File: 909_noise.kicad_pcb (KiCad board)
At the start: 2 copper layers, 30 x 20 mm, 20 parts, among them J1 Conn_01x02_Pin, J2 Conn_01x03_Pin, J3 3220-10-0300-00, SW1 PTS645SM43SMTR92 LFS, U1 STM32G030J6Mx, U2 L78L33ABUTR, U3 TLV7211A

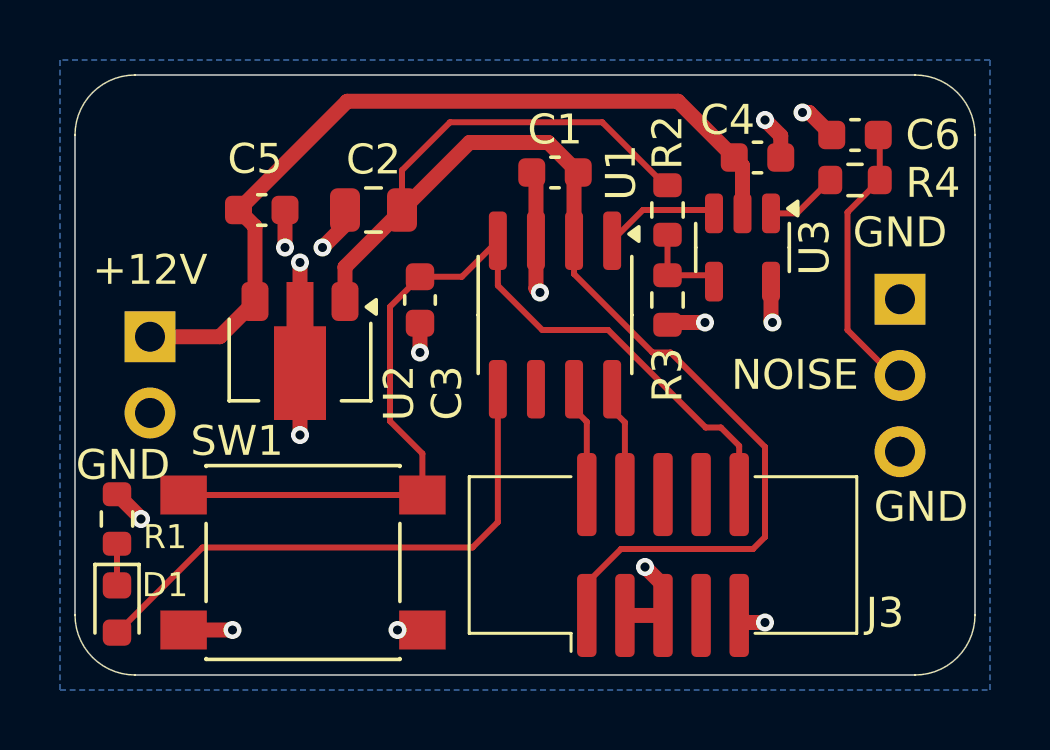
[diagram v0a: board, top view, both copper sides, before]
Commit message: cleanup footprint attributes between pcb and sch
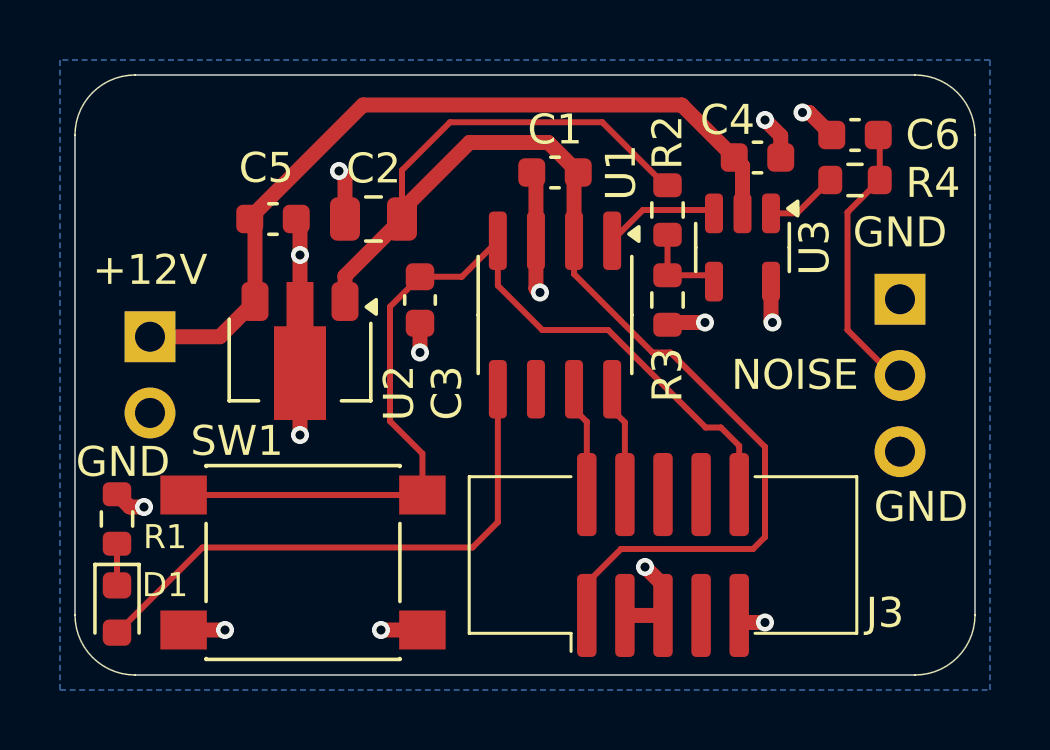
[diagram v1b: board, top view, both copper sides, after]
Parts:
- moved C5 0.48 mm to (51.6, 24.8)
- moved C2 0.30 mm to (55.0, 24.8)
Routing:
- net +12V: track 28.0 -> 27.2 mm
- net GND: track 26.8 -> 27.4 mm, vias 15 -> 14
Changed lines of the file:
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@@
 	(footprint "Capacitor_SMD:C_0603_1608Metric"
 		(layer "F.Cu")
-		(at 51.225 24.5 180)
+		(at 51.6 24.8 180)
 		(descr "Capacitor SMD 0603 (1608 Metric), square (rectangular) end terminal, IPC_7351 nominal, (Body size source: IPC-SM-782 page 76, https://www.pcb-3d.com/wordpress/wp-content/uploads/ipc-sm-782a_amendment_1_and_2.pdf), generated with kicad-footprint-generator")
 		(tags "capacitor")
@@
 	(footprint "Capacitor_SMD:C_0805_2012Metric"
 		(layer "F.Cu")
-		(at 54.95 24.5)
+		(at 54.95 24.8)
 		(descr "Capacitor SMD 0805 (2012 Metric), square (rectangular) end terminal, IPC_7351 nominal, (Body size source: IPC-SM-782 page 76, https://www.pcb-3d.com/wordpress/wp-content/uploads/ipc-sm-782a_amendment_1_and_2.pdf, https://docs.google.com/spreadsheets/d/1BsfQQcO9C6DZCsRaXUlFlo91Tg2WpOkGARC1WS5S8t0/edit?usp=sharing), generated with kicad-footprint-generator")
 		(tags "capacitor")
@@
 		(sheetname "Root")
 		(sheetfile "909_noise.kicad_sch")
-		(attr through_hole)
+		(attr exclude_from_pos_files exclude_from_bom allow_missing_courtyard)
 		(fp_poly
 			(pts
@@
 		)
 		(property "pin2" "GND"
-			(at 0.9 -4.275 0)
+			(at 0.9 -4.175 0)
 			(unlocked yes)
 			(layer "F.SilkS")
@@
 	)
 	(segment
-		(start 54 25)
-		(end 53.25 25.75)
+		(start 50 38.5)
+		(end 48.62 38.5)
 		(width 0.5)
 		(layer "F.Cu")
@@
 	)
 	(segment
-		(start 52.5 27.6375)
-		(end 52.5 26.25)
+		(start 68.2 26.8875)
+		(end 68.2 28.2)
 		(width 0.5)
 		(layer "F.Cu")
@@
 	)
 	(segment
-		(start 55.75 38.5)
-		(end 56.58 38.5)
+		(start 52.5 27.6375)
+		(end 52.5 32)
 		(width 0.5)
 		(layer "F.Cu")
@@
 	)
 	(segment
-		(start 54 24.5)
-		(end 54 25)
+		(start 69.25 21.25)
+		(end 69.475 21.25)
 		(width 0.5)
 		(layer "F.Cu")
@@
 	)
 	(segment
-		(start 68.2 26.8875)
-		(end 68.2 28.2)
+		(start 55.2 38.5)
+		(end 56.58 38.5)
 		(width 0.5)
 		(layer "F.Cu")
@@
 	)
 	(segment
-		(start 52.5 27.6375)
-		(end 52.5 32)
+		(start 54 24.8)
+		(end 53.95 24.8)
 		(width 0.5)
 		(layer "F.Cu")
@@
 	)
 	(segment
-		(start 69.25 21.25)
-		(end 69.475 21.25)
+		(start 64.6 37)
+		(end 64.6 38.015)
 		(width 0.5)
 		(layer "F.Cu")
@@
 	)
 	(segment
-		(start 64.6 37)
-		(end 64.6 38.015)
+		(start 60.365 27.115)
+		(end 60.5 27.25)
 		(width 0.5)
 		(layer "F.Cu")
@@
 	)
 	(segment
-		(start 60.365 27.115)
-		(end 60.5 27.25)
+		(start 52.5 27.6375)
+		(end 52.5 26)
 		(width 0.5)
 		(layer "F.Cu")
@@
 	)
 	(segment
-		(start 50.25 38.5)
-		(end 48.62 38.5)
-		(width 0.5)
-		(layer "F.Cu")
-		(net 1)
-	)
-	(segment
-		(start 47.2 34.775)
-		(end 46.4 33.975)
+		(start 47.3 34.4)
+		(end 46.825 34.4)
 		(width 0.5)
 		(layer "F.Cu")
@@
 	)
 	(segment
-		(start 47.2 34.8)
-		(end 47.2 34.775)
-		(width 0.5)
-		(layer "F.Cu")
-		(net 1)
-	)
-	(segment
 		(start 68.2 28.2)
 		(end 68.25 28.25)
@@
 	)
 	(segment
+		(start 54 24.8)
+		(end 54 23.4)
+		(width 0.5)
+		(layer "F.Cu")
+		(net 1)
+	)
+	(segment
 		(start 64.9 28.25)
 		(end 64.825 28.325)
@@
 	)
 	(segment
+		(start 54 23.4)
+		(end 53.8 23.2)
+		(width 0.5)
+		(layer "F.Cu")
+		(net 1)
+	)
+	(segment
+		(start 52.5 26)
+		(end 52.5 24.925)
+		(width 0.5)
+		(layer "F.Cu")
+		(net 1)
+	)
+	(segment
 		(start 69.475 21.25)
 		(end 70.225 22)
@@
 	)
 	(segment
-		(start 52 24.5)
-		(end 52 25.75)
+		(start 46.825 34.4)
+		(end 46.4 33.975)
+		(width 0.5)
+		(layer "F.Cu")
+		(net 1)
+	)
+	(segment
+		(start 52.5 24.925)
+		(end 52.375 24.8)
 		(width 0.5)
 		(layer "F.Cu")
@@
 	)
 	(via
-		(at 50.25 38.5)
+		(at 50 38.5)
 		(size 0.6)
 		(drill 0.3)
@@
 	)
 	(via
-		(at 52 25.75)
+		(at 53.8 23.2)
 		(size 0.6)
 		(drill 0.3)
@@
 	)
 	(via
-		(at 55.75 38.5)
+		(at 55.2 38.5)
 		(size 0.6)
 		(drill 0.3)
@@
 	)
 	(via
-		(at 47.2 34.8)
-		(size 0.6)
-		(drill 0.3)
-		(layers "F.Cu" "B.Cu")
-		(net 1)
-	)
-	(via
-		(at 53.25 25.75)
+		(at 47.3 34.4)
 		(size 0.6)
 		(drill 0.3)
@@
 	)
 	(via
-		(at 52.5 26.25)
+		(at 52.5 26)
 		(size 0.6)
 		(drill 0.3)
@@
 	)
 	(segment
+		(start 61.775 23.25)
+		(end 60.775 22.25)
+		(width 0.5)
+		(layer "F.Cu")
+		(net 2)
+	)
+	(segment
+		(start 64.675 23.675)
+		(end 64.75 23.675)
+		(width 0.2)
+		(layer "F.Cu")
+		(net 2)
+	)
+	(segment
 		(start 61.635 23.39)
 		(end 61.635 25.525)
@@
 	)
 	(segment
-		(start 62.575 21.575)
-		(end 64.675 23.675)
+		(start 55.9 24.8)
+		(end 55.9 23.175)
 		(width 0.2)
 		(layer "F.Cu")
@@
 	)
 	(segment
-		(start 61.775 23.25)
-		(end 60.775 22.25)
-		(width 0.5)
+		(start 57.5 21.575)
+		(end 62.575 21.575)
+		(width 0.2)
 		(layer "F.Cu")
 		(net 2)
 	)
 	(segment
-		(start 68 35.4)
-		(end 67.6 35.8)
-		(width 0.2)
+		(start 55.9 24.5)
+		(end 55.9 24.8)
+		(width 0.5)
 		(layer "F.Cu")
 		(net 2)
 	)
 	(segment
-		(start 64.85 29.25)
-		(end 68 32.4)
-		(width 0.2)
+		(start 58.15 22.25)
+		(end 55.9 24.5)
+		(width 0.5)
 		(layer "F.Cu")
 		(net 2)
 	)
 	(segment
-		(start 55.9 23.175)
-		(end 57.5 21.575)
+		(start 68 35.4)
+		(end 67.6 35.8)
 		(width 0.2)
 		(layer "F.Cu")
@@
 	)
 	(segment
-		(start 67.6 35.8)
-		(end 63.2 35.8)
+		(start 64.85 29.25)
+		(end 68 32.4)
 		(width 0.2)
 		(layer "F.Cu")
@@
 	)
 	(segment
-		(start 54 26.4)
-		(end 55.9 24.5)
-		(width 0.5)
+		(start 67.6 35.8)
+		(end 63.2 35.8)
+		(width 0.2)
 		(layer "F.Cu")
 		(net 2)
 	)
 	(segment
-		(start 57.5 21.575)
-		(end 62.575 21.575)
+		(start 62.575 21.575)
+		(end 64.675 23.675)
 		(width 0.2)
 		(layer "F.Cu")
@@
 	(segment
 		(start 54 27.55)
-		(end 54 26.4)
+		(end 54 26.7)
 		(width 0.5)
 		(layer "F.Cu")
@@
 	)
 	(segment
-		(start 68 32.4)
-		(end 68 35.4)
-		(width 0.2)
-		(layer "F.Cu")
-		(net 2)
-	)
-	(segment
 		(start 60.775 22.25)
 		(end 58.15 22.25)
@@
 	)
 	(segment
-		(start 55.9 24.5)
-		(end 55.9 23.175)
+		(start 68 32.4)
+		(end 68 35.4)
 		(width 0.2)
 		(layer "F.Cu")
@@
 	)
 	(segment
-		(start 58.15 22.25)
-		(end 55.9 24.5)
+		(start 54 26.7)
+		(end 55.9 24.8)
 		(width 0.5)
 		(layer "F.Cu")
@@
 	)
 	(segment
-		(start 64.675 23.675)
-		(end 64.75 23.675)
+		(start 55.9 23.175)
+		(end 57.5 21.575)
 		(width 0.2)
 		(layer "F.Cu")
@@
 	)
 	(segment
-		(start 51 25.05)
-		(end 50.45 24.5)
+		(start 65.225 21)
+		(end 66.975 22.75)
 		(width 0.5)
 		(layer "F.Cu")
@@
 	)
 	(segment
-		(start 65.1 20.875)
-		(end 66.975 22.75)
+		(start 54.6 21)
+		(end 65.225 21)
 		(width 0.5)
 		(layer "F.Cu")
@@
 	)
 	(segment
-		(start 54.075 20.875)
-		(end 65.1 20.875)
+		(start 51 27.55)
+		(end 51 24.975)
 		(width 0.5)
 		(layer "F.Cu")
@@
 	)
 	(segment
-		(start 51 27.55)
-		(end 51 25.05)
+		(start 50.825 24.8)
+		(end 50.825 24.775)
+		(width 0.5)
+		(layer "F.Cu")
+		(net 4)
+	)
+	(segment
+		(start 50.825 24.775)
+		(end 54.6 21)
 		(width 0.5)
 		(layer "F.Cu")
@@
 	)
 	(segment
-		(start 50.45 24.5)
-		(end 54.075 20.875)
+		(start 51 24.975)
+		(end 50.825 24.8)
 		(width 0.5)
 		(layer "F.Cu")

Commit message: tweak silk and footprint placement
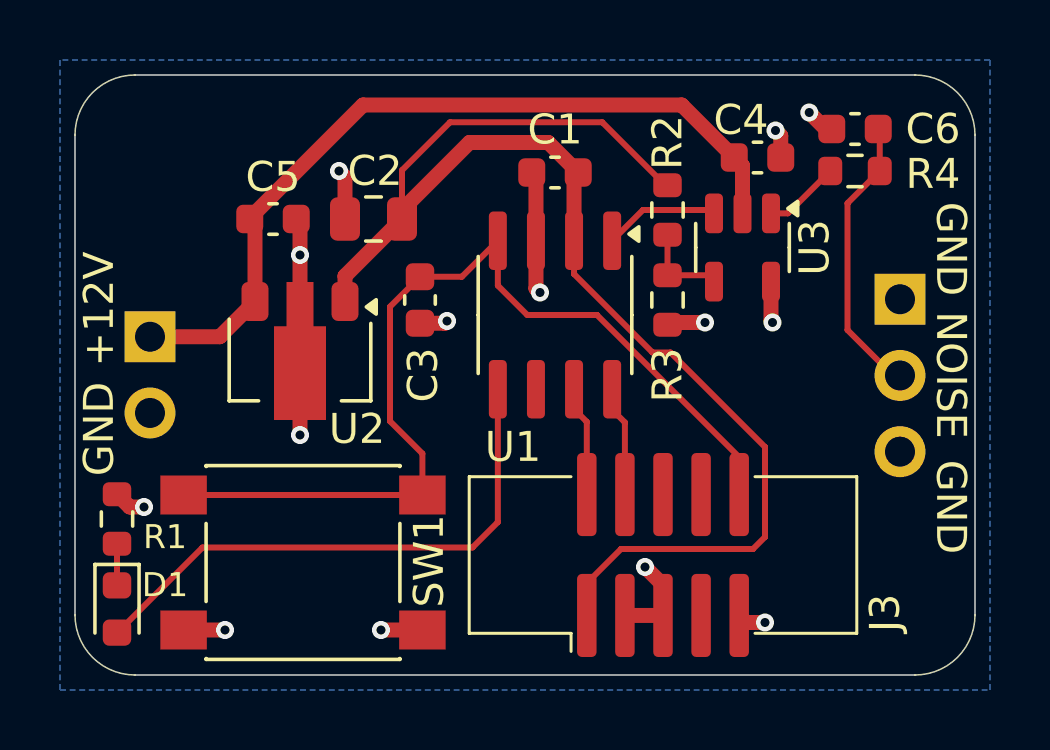
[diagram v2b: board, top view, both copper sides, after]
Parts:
- moved R4 0.30 mm to (71.0, 23.2)
- moved C6 0.20 mm to (71.0, 21.8)
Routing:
- net GND: track 27.4 -> 26.6 mm
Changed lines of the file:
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@@
 	(footprint "Capacitor_SMD:C_0603_1608Metric"
 		(layer "F.Cu")
-		(at 71 22)
+		(at 71 21.8)
 		(descr "Capacitor SMD 0603 (1608 Metric), square (rectangular) end terminal, IPC_7351 nominal, (Body size source: IPC-SM-782 page 76, https://www.pcb-3d.com/wordpress/wp-content/uploads/ipc-sm-782a_amendment_1_and_2.pdf), generated with kicad-footprint-generator")
 		(tags "capacitor")
@@
 		(tags "SPST Button Switch")
 		(property "Reference" "SW1"
-			(at 2.2 4.05 0)
+			(at -4.2 0.05 -90)
 			(layer "F.SilkS")
 			(effects
@@
 		(tags "capacitor")
 		(property "Reference" "C5"
-			(at 0.225 1.7 180)
+			(at 0 1.4 180)
 			(layer "F.SilkS")
 			(effects
@@
 				(font
 					(size 0.8 0.8)
-					(thickness 0.15)
+					(thickness 0.12)
 				)
 			)
@@
 		(descr "CNC Tech 3220-10-0300-00 2x05 1.27mm shrouded connector, ARM Debug compatible (https://www.cnctech.us/pdfs/3220-XX-0300-00_.pdf)")
 		(property "Reference" "J3"
-			(at -1.93 7.4 0)
+			(at -1.93 7.4 90)
 			(unlocked yes)
 			(layer "F.SilkS")
@@
 		(tags "capacitor")
 		(property "Reference" "C2"
-			(at 0 -1.68 0)
+			(at 0.05 -1.6 0)
 			(layer "F.SilkS")
 			(effects
@@
 		(tags "SOIC SO")
 		(property "Reference" "U1"
-			(at -4.75 -2.2 -90)
+			(at 4.4 1.4 0)
 			(layer "F.SilkS")
 			(effects
@@
 		(tags "capacitor")
 		(property "Reference" "C4"
-			(at 1 1.25 180)
+			(at 0.55 1.25 180)
 			(layer "F.SilkS")
 			(effects
@@
 	(footprint "Resistor_SMD:R_0603_1608Metric"
 		(layer "F.Cu")
-		(at 71 23.5)
+		(at 71 23.2)
 		(descr "Resistor SMD 0603 (1608 Metric), square (rectangular) end terminal, IPC_7351 nominal, (Body size source: IPC-SM-782 page 72, https://www.pcb-3d.com/wordpress/wp-content/uploads/ipc-sm-782a_amendment_1_and_2.pdf), generated with kicad-footprint-generator")
 		(tags "resistor")
@@
 		(tags "SOT-89-3")
 		(property "Reference" "U2"
-			(at 1.1 -3.3 90)
+			(at 2.3 -1.9 180)
 			(layer "F.SilkS")
 			(effects
@@
 				(font
 					(size 0.8 0.8)
-					(thickness 0.15)
+					(thickness 0.12)
 				)
 			)
@@
 		(tags "capacitor")
 		(property "Reference" "C3"
-			(at -3.1 0.9 -90)
+			(at -2.5 0.1 -90)
 			(layer "F.SilkS")
 			(effects
@@
 		)
 		(property "pin1" "+12V"
-			(at 0 2.225 0)
+			(at 1.7 0.925 90)
 			(unlocked yes)
 			(layer "F.SilkS")
@@
 		)
 		(property "pin2" "GND"
-			(at 0.9 -4.175 0)
+			(at 1.7 -3.075 90)
 			(unlocked yes)
 			(layer "F.SilkS")
@@
 		)
 		(property "pin1" "GND"
-			(at 0 2.225 0)
+			(at -1.7 1.675 -90)
 			(unlocked yes)
 			(layer "F.SilkS")
@@
 		)
 		(property "pin2" "NOISE"
-			(at 3.5 -2.525 0)
+			(at -1.7 -2.525 -90)
 			(unlocked yes)
 			(layer "F.SilkS")
@@
 		)
 		(property "pin3" "GND"
-			(at -0.7 -6.925 0)
+			(at -1.7 -6.925 -90)
 			(unlocked yes)
 			(layer "F.SilkS")
@@
 	)
 	(segment
+		(start 56.5 28.275)
+		(end 57.325 28.275)
+		(width 0.5)
+		(layer "F.Cu")
+		(net 1)
+	)
+	(segment
 		(start 68.2 26.8875)
 		(end 68.2 28.2)
@@
 	)
 	(segment
-		(start 69.25 21.25)
-		(end 69.475 21.25)
+		(start 68.525 22.025)
+		(end 68.525 22.75)
+		(width 0.5)
+		(layer "F.Cu")
+		(net 1)
+	)
+	(segment
+		(start 70.025 21.8)
+		(end 70.225 21.8)
 		(width 0.5)
 		(layer "F.Cu")
@@
 	)
 	(segment
-		(start 68 21.5)
-		(end 68.525 22.025)
+		(start 60.365 23.39)
+		(end 60.365 25.525)
 		(width 0.5)
 		(layer "F.Cu")
@@
 	)
 	(segment
-		(start 60.365 23.39)
-		(end 60.365 25.525)
+		(start 68.2 28.2)
+		(end 68.25 28.25)
 		(width 0.5)
 		(layer "F.Cu")
@@
 	)
 	(segment
-		(start 68.2 28.2)
-		(end 68.25 28.25)
+		(start 68.35 21.85)
+		(end 68.525 22.025)
 		(width 0.5)
 		(layer "F.Cu")
@@
 	)
 	(segment
+		(start 57.325 28.275)
+		(end 57.4 28.2)
+		(width 0.5)
+		(layer "F.Cu")
+		(net 1)
+	)
+	(segment
 		(start 67.375 38.25)
 		(end 67.14 38.015)
@@
 	)
 	(segment
-		(start 68.525 22.025)
-		(end 68.525 22.75)
+		(start 69.475 21.25)
+		(end 70.025 21.8)
 		(width 0.5)
 		(layer "F.Cu")
@@
 	)
 	(segment
-		(start 69.475 21.25)
-		(end 70.225 22)
-		(width 0.5)
-		(layer "F.Cu")
-		(net 1)
-	)
-	(segment
-		(start 56.5 28.275)
-		(end 56.5 29.25)
-		(width 0.5)
-		(layer "F.Cu")
-		(net 1)
-	)
-	(segment
 		(start 66 28.25)
 		(end 64.9 28.25)
@@
 	)
 	(via
-		(at 56.5 29.25)
+		(at 57.4 28.2)
 		(size 0.6)
 		(drill 0.3)
@@
 	)
 	(via
-		(at 69.25 21.25)
+		(at 69.475 21.25)
 		(size 0.6)
 		(drill 0.3)
@@
 	)
 	(via
-		(at 68 21.5)
+		(at 68.35 21.85)
 		(size 0.6)
 		(drill 0.3)
@@
 	)
 	(segment
-		(start 67.14 32.36)
-		(end 66.53 31.75)
-		(width 0.2)
-		(layer "F.Cu")
-		(net 3)
-	)
-	(segment
-		(start 62.772776 28.5)
-		(end 60.575736 28.5)
+		(start 60.075736 28)
+		(end 59.095 27.019264)
 		(width 0.2)
 		(layer "F.Cu")
@@
 	)
 	(segment
-		(start 55.5 27.725)
-		(end 56.5 26.725)
+		(start 62.4 28)
+		(end 60.075736 28)
 		(width 0.2)
 		(layer "F.Cu")
@@
 	)
 	(segment
-		(start 59.095 27.019264)
-		(end 59.095 25.525)
+		(start 55.5 27.725)
+		(end 56.5 26.725)
 		(width 0.2)
 		(layer "F.Cu")
@@
 	)
 	(segment
-		(start 60.575736 28.5)
-		(end 59.095 27.019264)
+		(start 59.095 27.019264)
+		(end 59.095 25.525)
 		(width 0.2)
 		(layer "F.Cu")
@@
 	)
 	(segment
-		(start 66.022776 31.75)
-		(end 62.772776 28.5)
-		(width 0.2)
-		(layer "F.Cu")
-		(net 3)
-	)
-	(segment
-		(start 55.5 31.54)
-		(end 55.5 27.725)
+		(start 67.14 32.74)
+		(end 62.4 28)
 		(width 0.2)
 		(layer "F.Cu")
@@
 	)
 	(segment
-		(start 66.53 31.75)
-		(end 66.022776 31.75)
+		(start 67.14 33.985)
+		(end 67.14 32.74)
 		(width 0.2)
 		(layer "F.Cu")
@@
 	)
 	(segment
-		(start 67.14 33.985)
-		(end 67.14 32.36)
+		(start 55.5 31.54)
+		(end 55.5 27.725)
 		(width 0.2)
 		(layer "F.Cu")
@@
 	)
 	(segment
-		(start 68.2 24.6125)
-		(end 69.0625 24.6125)
+		(start 68.7625 24.6125)
+		(end 70.175 23.2)
 		(width 0.2)
 		(layer "F.Cu")
@@
 	)
 	(segment
-		(start 69.0625 24.6125)
-		(end 70.175 23.5)
+		(start 68.2 24.6125)
+		(end 68.7625 24.6125)
 		(width 0.2)
 		(layer "F.Cu")
@@
 	)
 	(segment
-		(start 72.265 30.015)
-		(end 72.5 30.015)
+		(start 71.825 23.2)
+		(end 70.75 24.275)
 		(width 0.2)
 		(layer "F.Cu")
@@
 	)
 	(segment
-		(start 71.825 23.5)
-		(end 71.825 22.05)
+		(start 70.75 28.5)
+		(end 72.265 30.015)
 		(width 0.2)
 		(layer "F.Cu")
@@
 	)
 	(segment
-		(start 70.75 28.5)
-		(end 72.265 30.015)
+		(start 71.825 21.85)
+		(end 71.775 21.8)
 		(width 0.2)
 		(layer "F.Cu")
@@
 	)
 	(segment
-		(start 71.825 22.05)
-		(end 71.775 22)
+		(start 72.265 30.015)
+		(end 72.5 30.015)
 		(width 0.2)
 		(layer "F.Cu")
@@
 	)
 	(segment
-		(start 71.825 23.5)
-		(end 70.75 24.575)
+		(start 71.825 23.2)
+		(end 71.825 21.85)
 		(width 0.2)
 		(layer "F.Cu")
@@
 	)
 	(segment
-		(start 70.75 24.575)
+		(start 70.75 24.275)
 		(end 70.75 28.5)
 		(width 0.2)

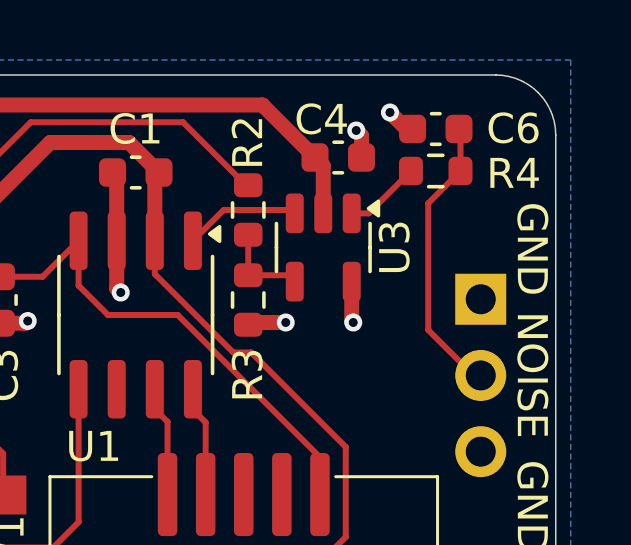
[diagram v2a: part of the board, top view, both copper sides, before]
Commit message: fix overlapping courtyards
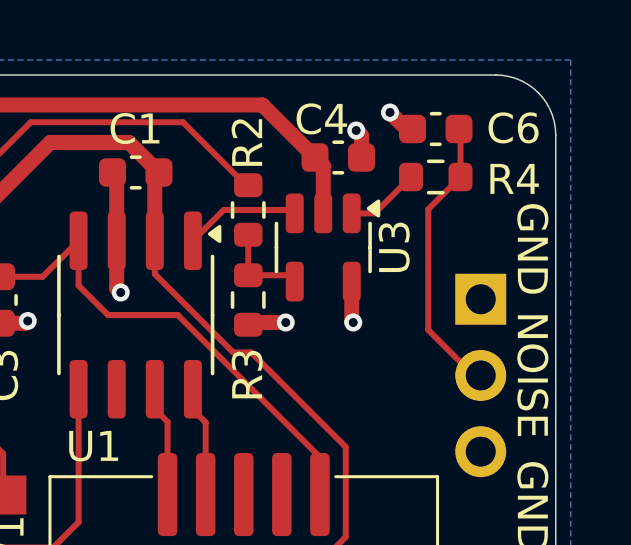
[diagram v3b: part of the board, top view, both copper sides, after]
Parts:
- moved R4 0.20 mm to (71.0, 23.4)
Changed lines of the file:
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@@
 	(footprint "Resistor_SMD:R_0603_1608Metric"
 		(layer "F.Cu")
-		(at 71 23.2)
+		(at 71 23.4)
 		(descr "Resistor SMD 0603 (1608 Metric), square (rectangular) end terminal, IPC_7351 nominal, (Body size source: IPC-SM-782 page 72, https://www.pcb-3d.com/wordpress/wp-content/uploads/ipc-sm-782a_amendment_1_and_2.pdf), generated with kicad-footprint-generator")
 		(tags "resistor")
@@
 	)
 	(segment
-		(start 68.7625 24.6125)
-		(end 70.175 23.2)
+		(start 68.2 24.6125)
+		(end 68.9625 24.6125)
 		(width 0.2)
 		(layer "F.Cu")
@@
 	)
 	(segment
-		(start 68.2 24.6125)
-		(end 68.7625 24.6125)
+		(start 68.9625 24.6125)
+		(end 70.175 23.4)
 		(width 0.2)
 		(layer "F.Cu")
@@
 	)
 	(segment
-		(start 71.825 23.2)
-		(end 70.75 24.275)
+		(start 72.265 30.015)
+		(end 72.5 30.015)
 		(width 0.2)
 		(layer "F.Cu")
@@
 	)
 	(segment
-		(start 72.265 30.015)
-		(end 72.5 30.015)
+		(start 70.75 24.475)
+		(end 70.75 28.5)
 		(width 0.2)
 		(layer "F.Cu")
@@
 	)
 	(segment
-		(start 71.825 23.2)
+		(start 71.825 23.4)
 		(end 71.825 21.85)
 		(width 0.2)
@@
 	)
 	(segment
-		(start 70.75 24.275)
-		(end 70.75 28.5)
+		(start 71.825 23.4)
+		(end 70.75 24.475)
 		(width 0.2)
 		(layer "F.Cu")

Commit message: swap symbols for specified symbols from dblib
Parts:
- C2: value 4.7u -> 4.7μ
- D1: value green -> Green
- J1: value Conn_01x02_Pin -> 1x2 Header
- J2: value Conn_01x03_Pin -> 1x3 Header
- LOGO1: value CC-BY-SA_0.33in -> CC-BY-SA
- LOGO2: value Logo_MadeWithKiCad -> Made With KiCad
- U1: value STM32G030J6Mx -> STM32G030J6M6
- U3: value TLV7211A -> TLV7211AIDBVR
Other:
- board text added: "+12V"
- board text added: "GND"
- board text added: "NOISE"
